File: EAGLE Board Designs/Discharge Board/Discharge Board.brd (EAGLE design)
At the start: 62.8 x 76.9 mm, 25 parts, among them J100 CONNECTOR-2_MICROFIT_SMD_RIGH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, J101 CONNECTOR-2_MICROFIT_SMD_RIGH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, K1 RELAY_SPST_NC_POLARIZED_D_24

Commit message: Update Discharge Board.brd
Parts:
- moved D100 1.41 mm to (25.3, 32.4)
- moved J100 1.41 mm to (54.5, 38.7)
- moved J101 1.41 mm to (8.78, 38.7)
- moved K1 1.41 mm to (25.3, 38.7)
- moved R1 1.41 mm to (10.1, 38.7)
- moved R2 1.41 mm to (40.5, 38.7)
- moved R3 1.41 mm to (53.2, 38.7)
- moved U$1 1.41 mm to (6.95, 47.8)
- moved U$12 1.41 mm to (42.5, 47.5)
- moved U$2 1.41 mm to (20.4, 29.5)
- moved U$3 1.41 mm to (6.95, 51.3)
- moved U$5 1.41 mm to (32.1, 33.3)
- moved U$6 1.41 mm to (36.2, 33.3)
- moved U$8 1.41 mm to (42.5, 47.5)
- moved U$13 1.41 mm to (42.8, 30.0)
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
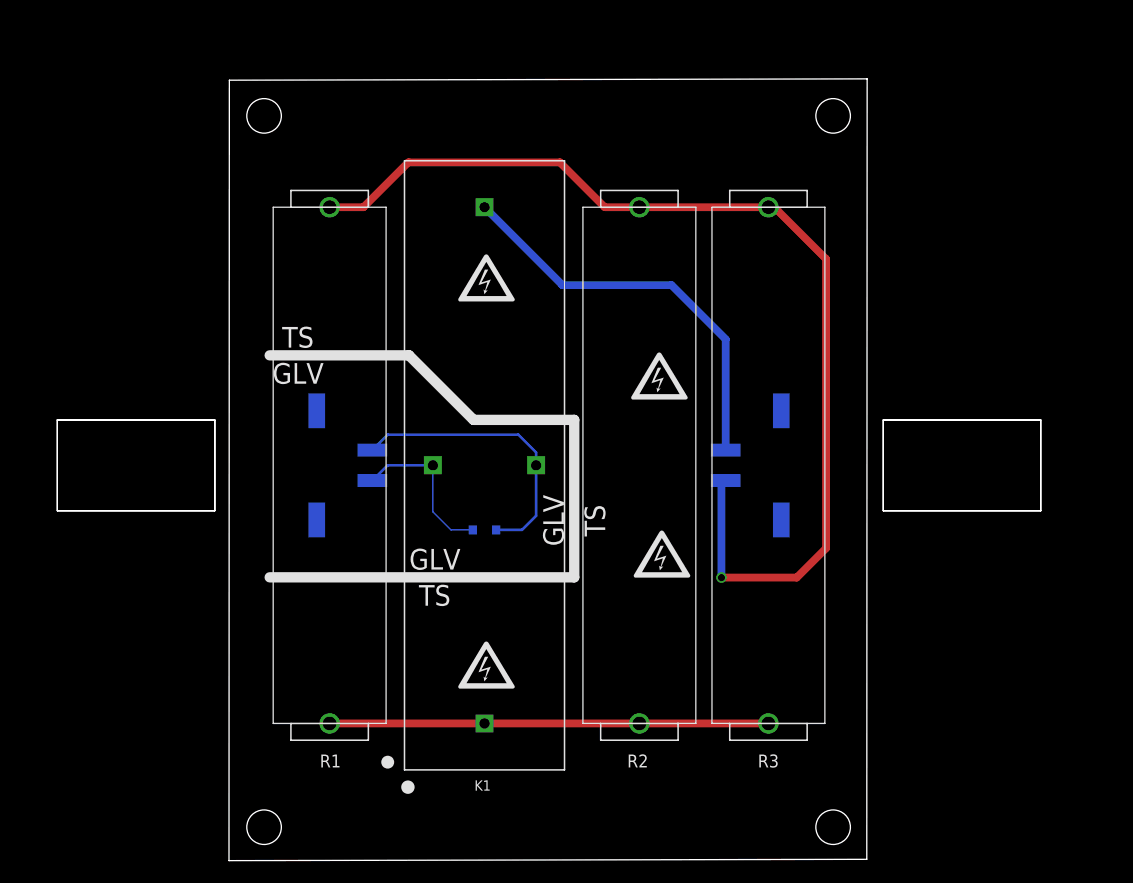
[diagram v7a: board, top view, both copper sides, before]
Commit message: adjusted to so all mounting holes are 70mm apart
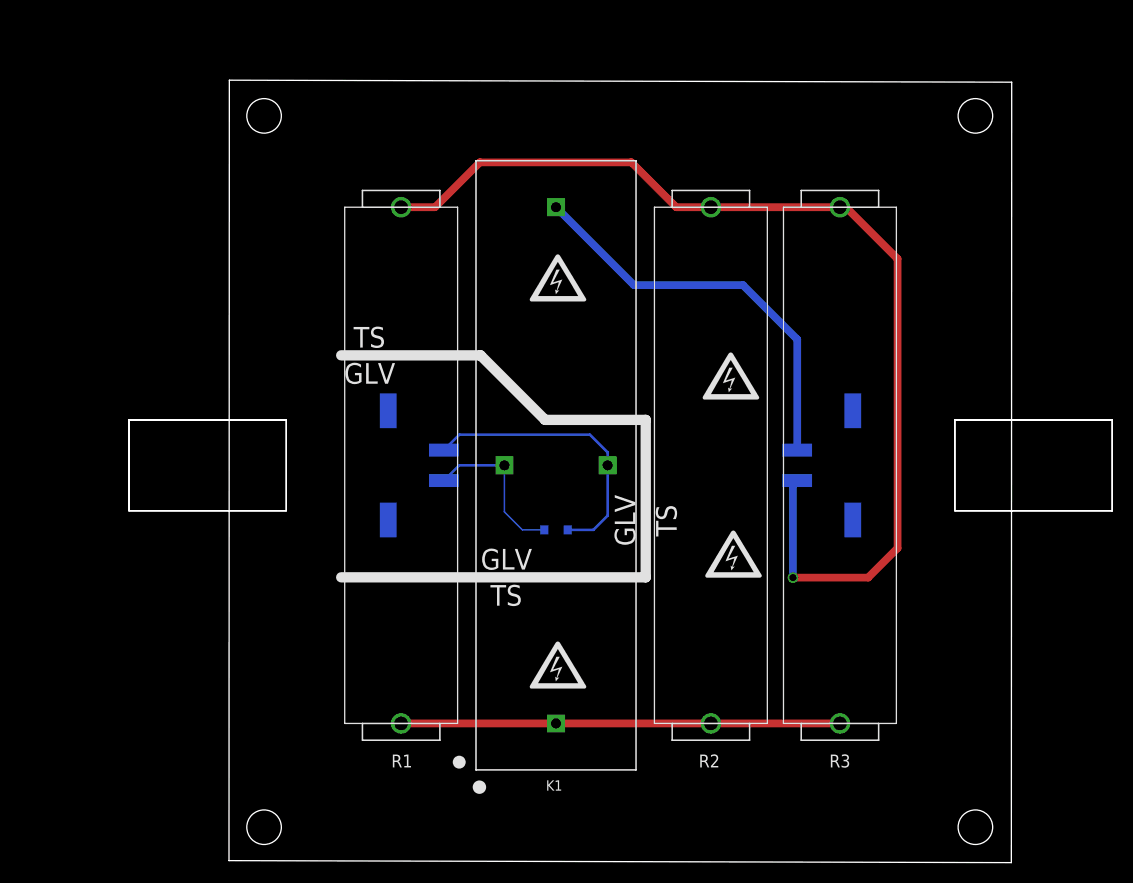
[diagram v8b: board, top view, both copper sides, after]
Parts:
- moved U$16 14.0 mm to (73.6, 3.10)
- moved U$18 14.0 mm to (73.6, 73.1)
- moved R3 7.04 mm to (60.3, 38.7)
- moved U$10 7.04 mm to (32.5, 57.2)
- moved U$11 7.04 mm to (32.5, 57.2)
- moved U$14 7.04 mm to (32.5, 19.1)
- moved U$7 7.04 mm to (32.5, 19.1)
- moved J101 7.04 mm to (15.8, 38.7)
- moved D100 7.04 mm to (32.3, 32.4)
- moved J100 7.04 mm to (61.5, 38.7)
- moved K1 7.04 mm to (32.3, 38.7)
- moved R1 7.04 mm to (17.1, 38.7)
- moved R2 7.04 mm to (47.6, 38.7)
- moved U$1 7.04 mm to (14.0, 47.8)
- moved U$12 7.04 mm to (49.5, 47.5)
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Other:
- board size 62.8 x 76.9 mm -> 77 x 77 mm
